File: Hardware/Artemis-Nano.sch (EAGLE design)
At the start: 65 parts, among them J10 USB-C, J11 CORTEX_DEBUG, U1 ARTEMIS_MODULESMD, U2 MCP73831, U3 3.3V, U6 CH340E_MSOP10, Y2 32.768kHz

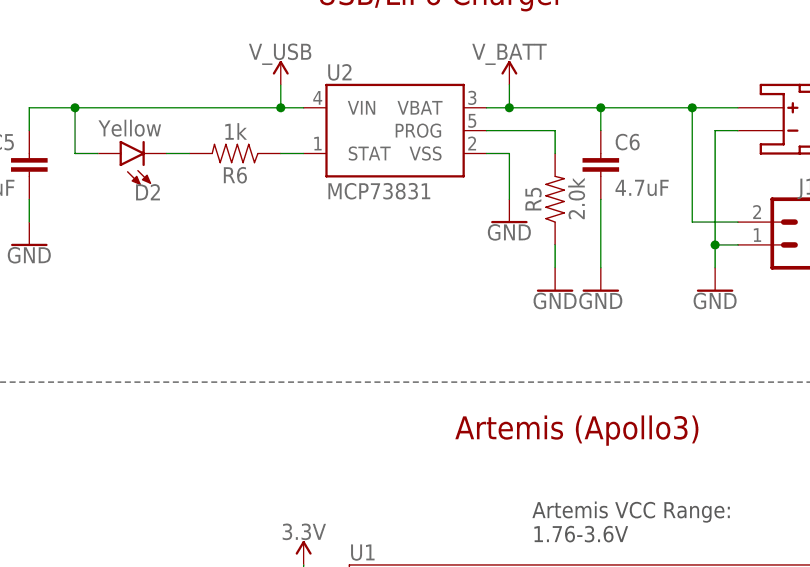
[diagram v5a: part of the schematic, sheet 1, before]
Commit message: Adding charge rate to sch
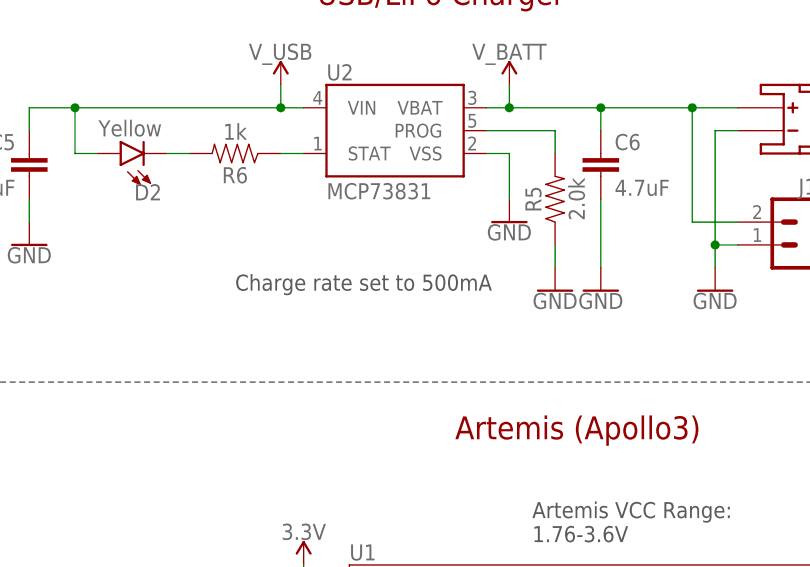
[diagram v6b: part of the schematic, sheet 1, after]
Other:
- note added: "Charge rate set to 500mA"
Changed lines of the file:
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@@
 <text x="76.2" y="119.38" size="1.778" layer="97">Artemis VCC Range:
 1.76-3.6V</text>
+<text x="43.18" y="147.32" size="1.778" layer="97" ratio="15">Charge rate set to 500mA</text>
 </plain>
 <instances>

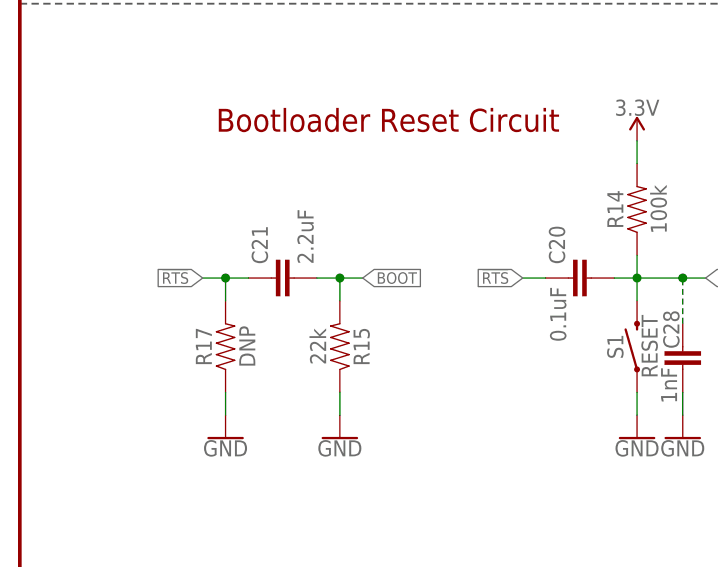
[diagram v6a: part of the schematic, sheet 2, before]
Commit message: Modify BL reset circuit to work with POR, SBL, and SVL
RTS doesn't like a 10k pull down. Remove R17. Increased R15 to 220k and reduced C21 to 0.1uF to maintain same RC time constant. Works for POR, SBL, and SVL.
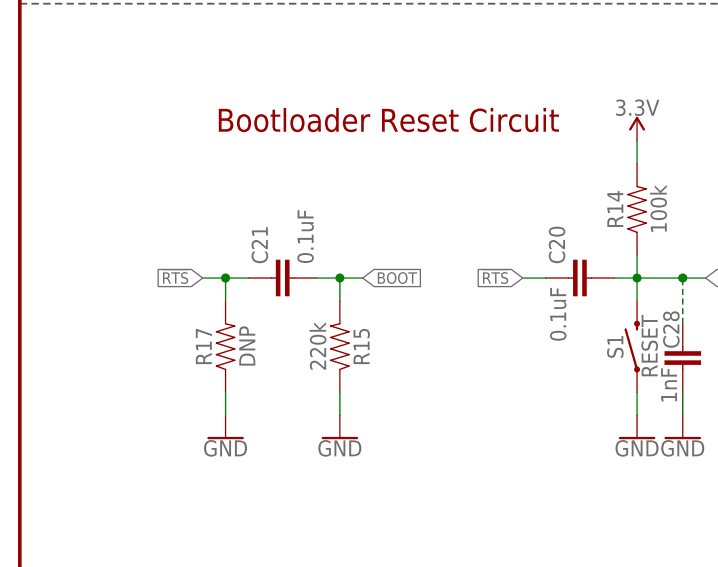
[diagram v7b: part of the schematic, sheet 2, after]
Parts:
- C21: value 2.2uF -> 0.1uF; device SparkFun-Capacitors:2.2UF-0603-10V-20% -> SparkFun-Capacitors:0.1UF-0603-25V-5%
- R15: value 22k -> 220k; device SparkFun-Resistors:22KOHM-0603-1/10W-1% -> SparkFun-Resistors:220KOHM-0603-1/10W-1%
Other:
- note added: "6V Max VIN / VUSB / VBATT"
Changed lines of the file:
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@@
 <?xml version="1.0" encoding="utf-8"?>
 <!DOCTYPE eagle SYSTEM "eagle.dtd">
-<eagle version="9.3.0">
+<eagle version="9.4.0">
 <drawing>
 <settings>
@@
 <part name="C20" library="SparkFun-Capacitors" deviceset="0.1UF" device="-0603-25V-5%" value="0.1uF"/>
 <part name="GND41" library="SparkFun-PowerSymbols" deviceset="GND" device=""/>
-<part name="R15" library="SparkFun-Resistors" deviceset="22KOHM" device="-0603-1/10W-1%" value="22k"/>
-<part name="C21" library="SparkFun-Capacitors" deviceset="2.2UF" device="-0603-10V-20%" value="2.2uF"/>
+<part name="R15" library="SparkFun-Resistors" deviceset="220KOHM" device="-0603-1/10W-1%" value="220k"/>
+<part name="C21" library="SparkFun-Capacitors" deviceset="0.1UF" device="-0603-25V-5%" value="0.1uF"/>
 <part name="R17" library="SparkFun-Resistors" deviceset="1MOHM" device="-0603-1/4W-5%" value="DNP"/>
 <part name="GND44" library="SparkFun-PowerSymbols" deviceset="GND" device=""/>
@@
 1.76-3.6V</text>
 <text x="43.18" y="147.32" size="1.778" layer="97" ratio="15">Charge rate set to 500mA</text>
+<text x="128.524" y="173.736" size="1.778" layer="97" ratio="15">6V Max VIN / VUSB / VBATT</text>
 </plain>
 <instances>
